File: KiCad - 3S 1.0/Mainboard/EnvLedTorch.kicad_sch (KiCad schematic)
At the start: 73 parts, among them J1 USB_C_Receptacle_USB2.0, J101 Conn_01x02, J102 Conn_01x02, Q1 BSP89, Q2 BSP89, Q3 BSP89, Q4 AO3401A, Q5 AO3401A, SW101 SW_SPST, U1 HY2213, U101 TPS565208, U102 TPS92200, U2 HY2213, U3 HY2213, U4 MT3608, U9 8254

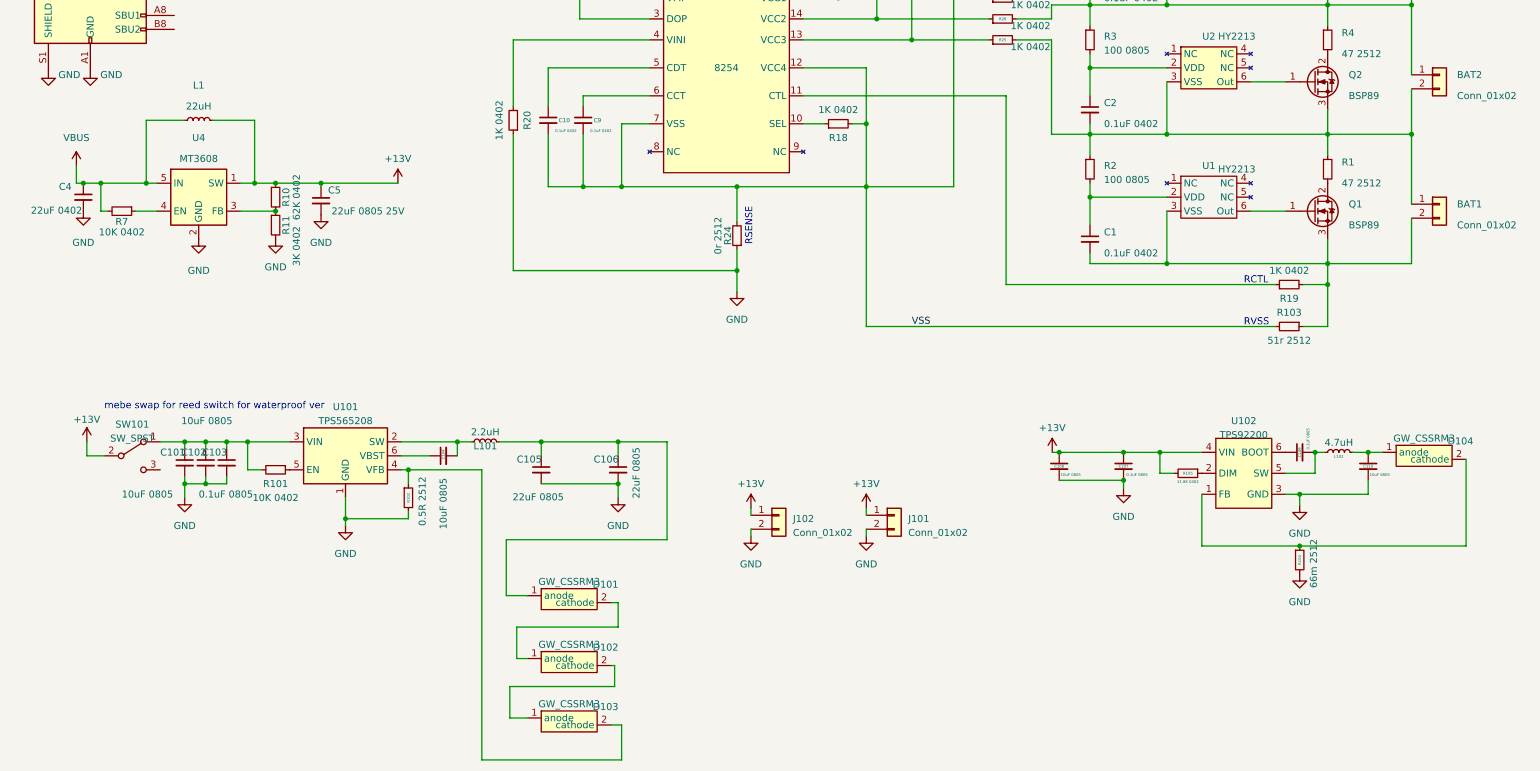
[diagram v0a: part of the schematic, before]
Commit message: broke up 3SV1 into two separate boards (unfinished work)
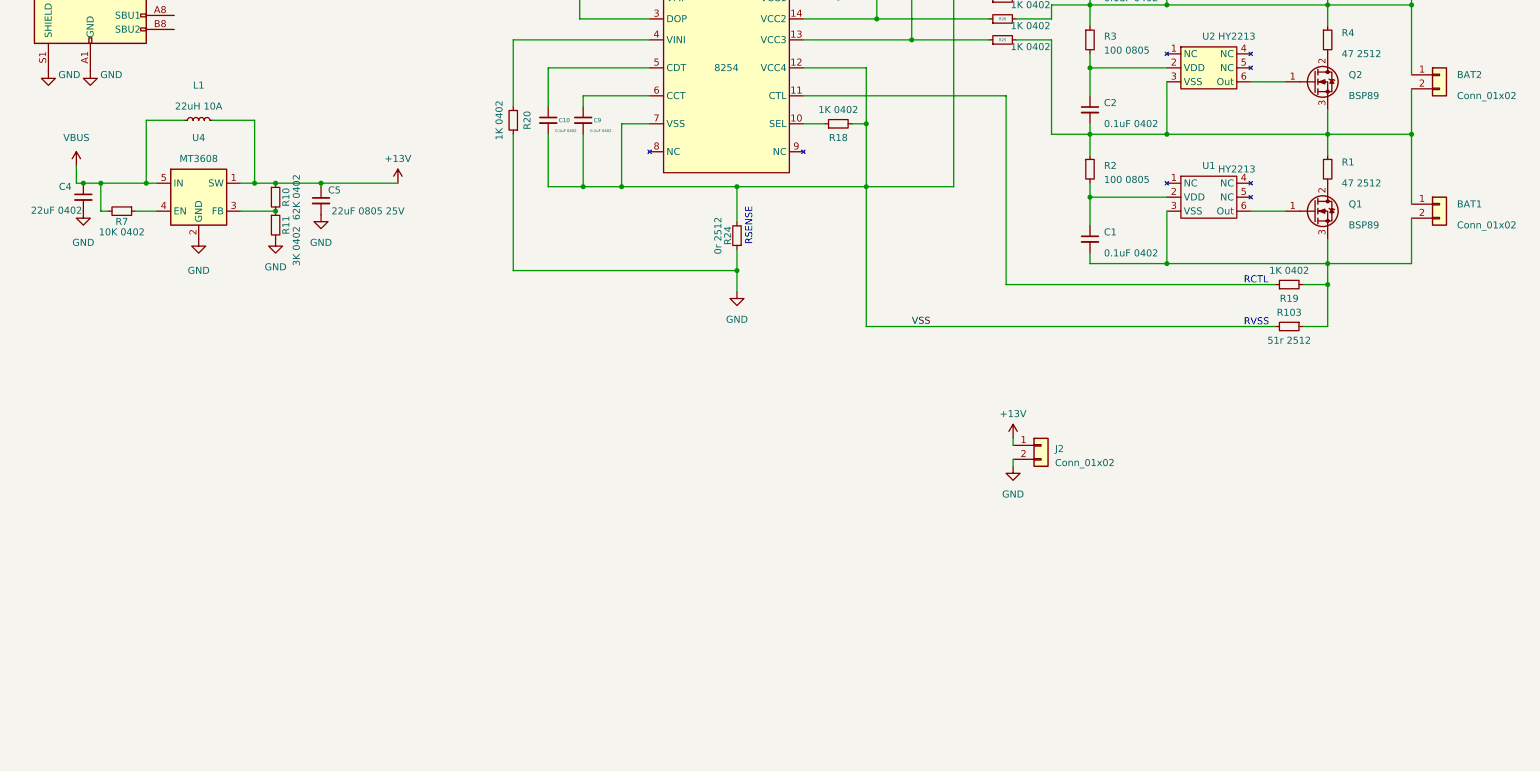
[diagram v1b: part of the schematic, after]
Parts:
- removed C101, C102, C104, C108, C110: 10uF 0805, Capacitor_SMD:C_0805_2012Metric, symbol Device:C_Small
- removed C103, C107, C109: 0.1uF 0805, Capacitor_SMD:C_0805_2012Metric, symbol Device:C_Small
- removed C105, C106: 22uF 0805, Capacitor_SMD:C_0805_2012Metric, symbol Device:C_Small
- removed D101, D102, D103, D104: GW_CSSRM3, GW_CSSRM3:GW_CSSRM3, symbol GW CSSRM3:GW_CSSRM3
- removed J101, J102: Conn_01x02, Connector_Wire:SolderWire-2sqmm_1x02_P7.8mm_D2mm_OD3.9mm, symbol Connector_Generic:Conn_01x02
- removed L101: 2.2uH, Inductor_SMD:L_Sunlord_MWSA0402S, symbol Device:L_Small
- removed L102: 4.7uH, Inductor_SMD:L_Sunlord_MWSA0402S, symbol Device:L_Small
- removed R101: 10K 0402, Resistor_SMD:R_0402_1005Metric, symbol Device:R_Small
- removed R102: 0.5R 2512, Resistor_SMD:R_2512_6332Metric, symbol Device:R_Small
- removed R104: 66m 2512, Resistor_SMD:R_2512_6332Metric, symbol Device:R_Small
- removed R105: 11.8K 0402, Resistor_SMD:R_0402_1005Metric, symbol Device:R_Small
- removed SW101: SW_SPST, Button_Switch_SMD:SW_SPDT_PCM12, symbol Switch:SW_SPDT
- removed U101: TPS565208, Package_TO_SOT_SMD:SOT-23-6, symbol Regulator_Switching:TPS565208
- removed U102: TPS92200, Package_TO_SOT_SMD:SOT-23-6, symbol TPS92200:TPS92200
- added J2: Conn_01x02, Connector_Wire:SolderWire-2sqmm_1x02_P7.8mm_D2mm_OD3.9mm, symbol Connector_Generic:Conn_01x02
- L1: value 22uH -> 22uH 10A; footprint Inductor_SMD:L_Sunlord_MWSA0402S -> Inductor_SMD:L_Sunlord_MWSA0605S
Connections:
- net +12V: now also J2.1 (Pin_1)
- net GND: now also J2.2 (Pin_2)
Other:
- note removed: "mebe swap for reed switch for waterproof ver"

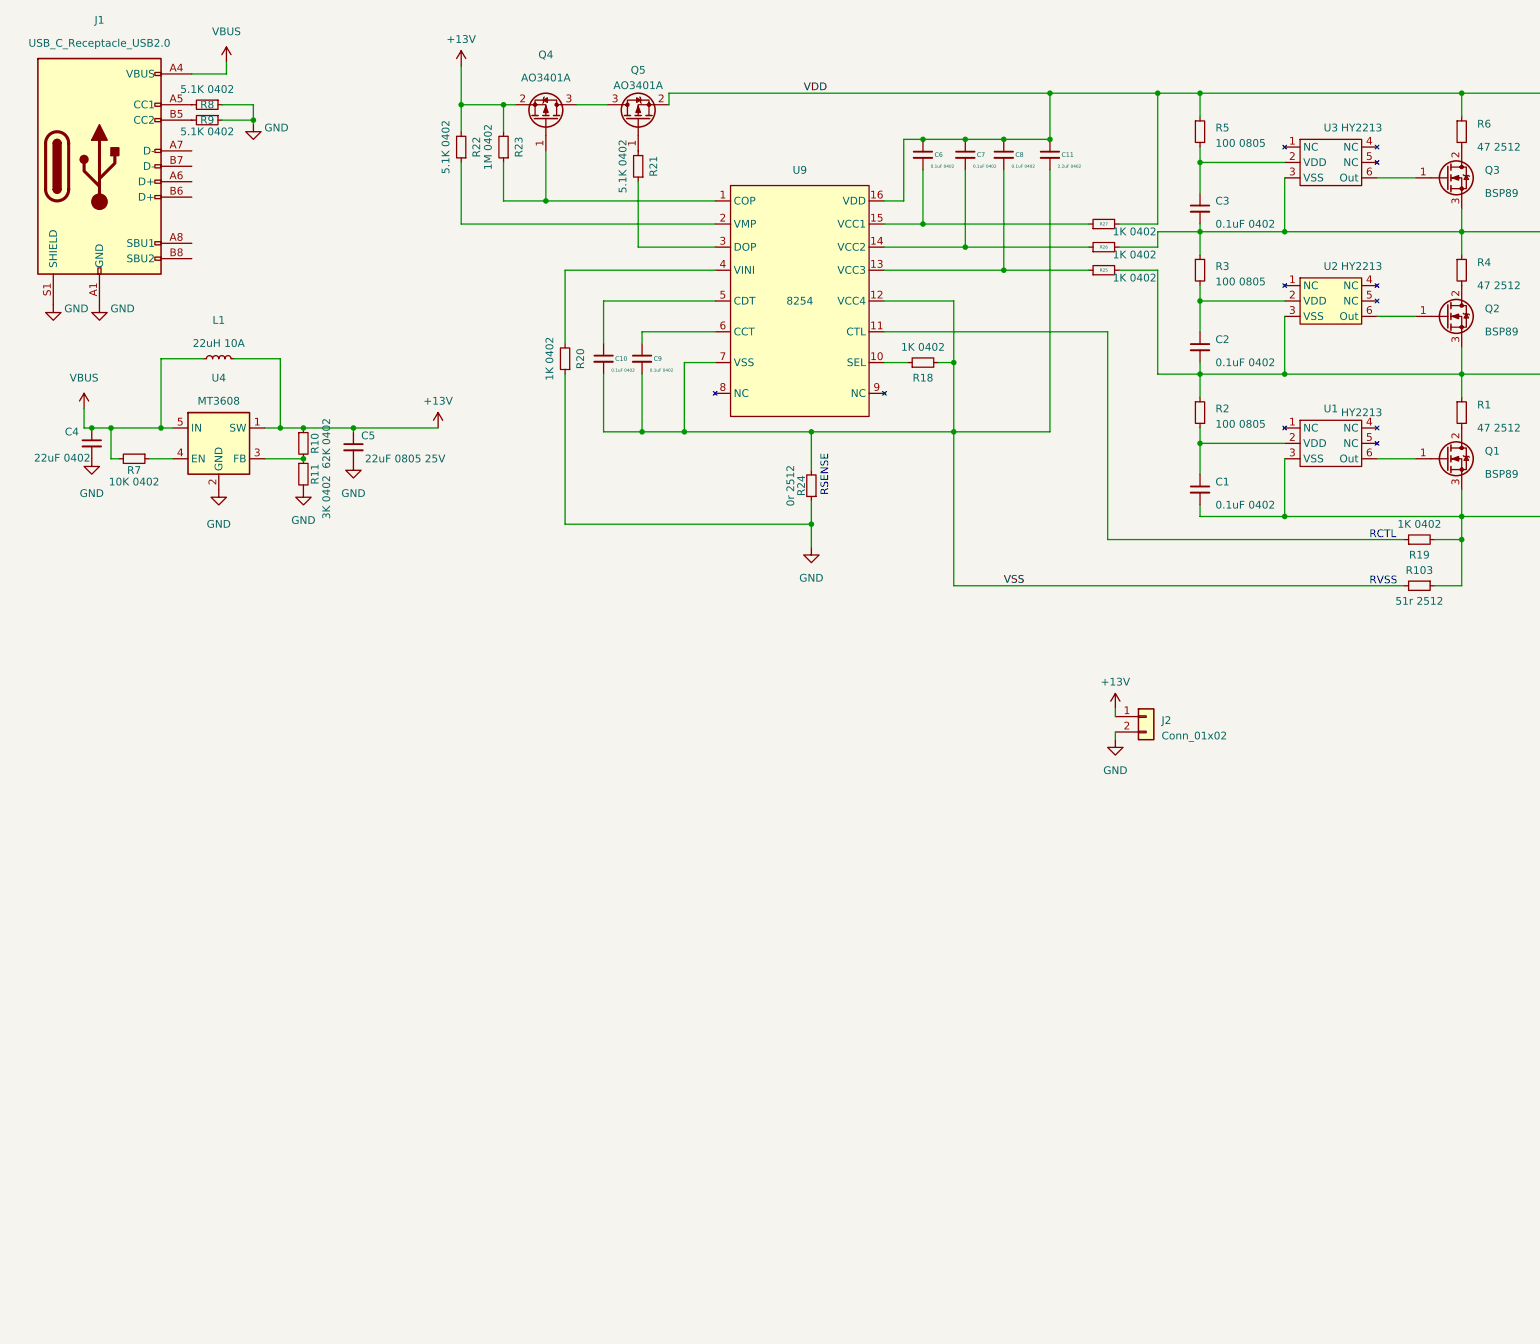
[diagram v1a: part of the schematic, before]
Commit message: started work on adding USB PD 100W support.
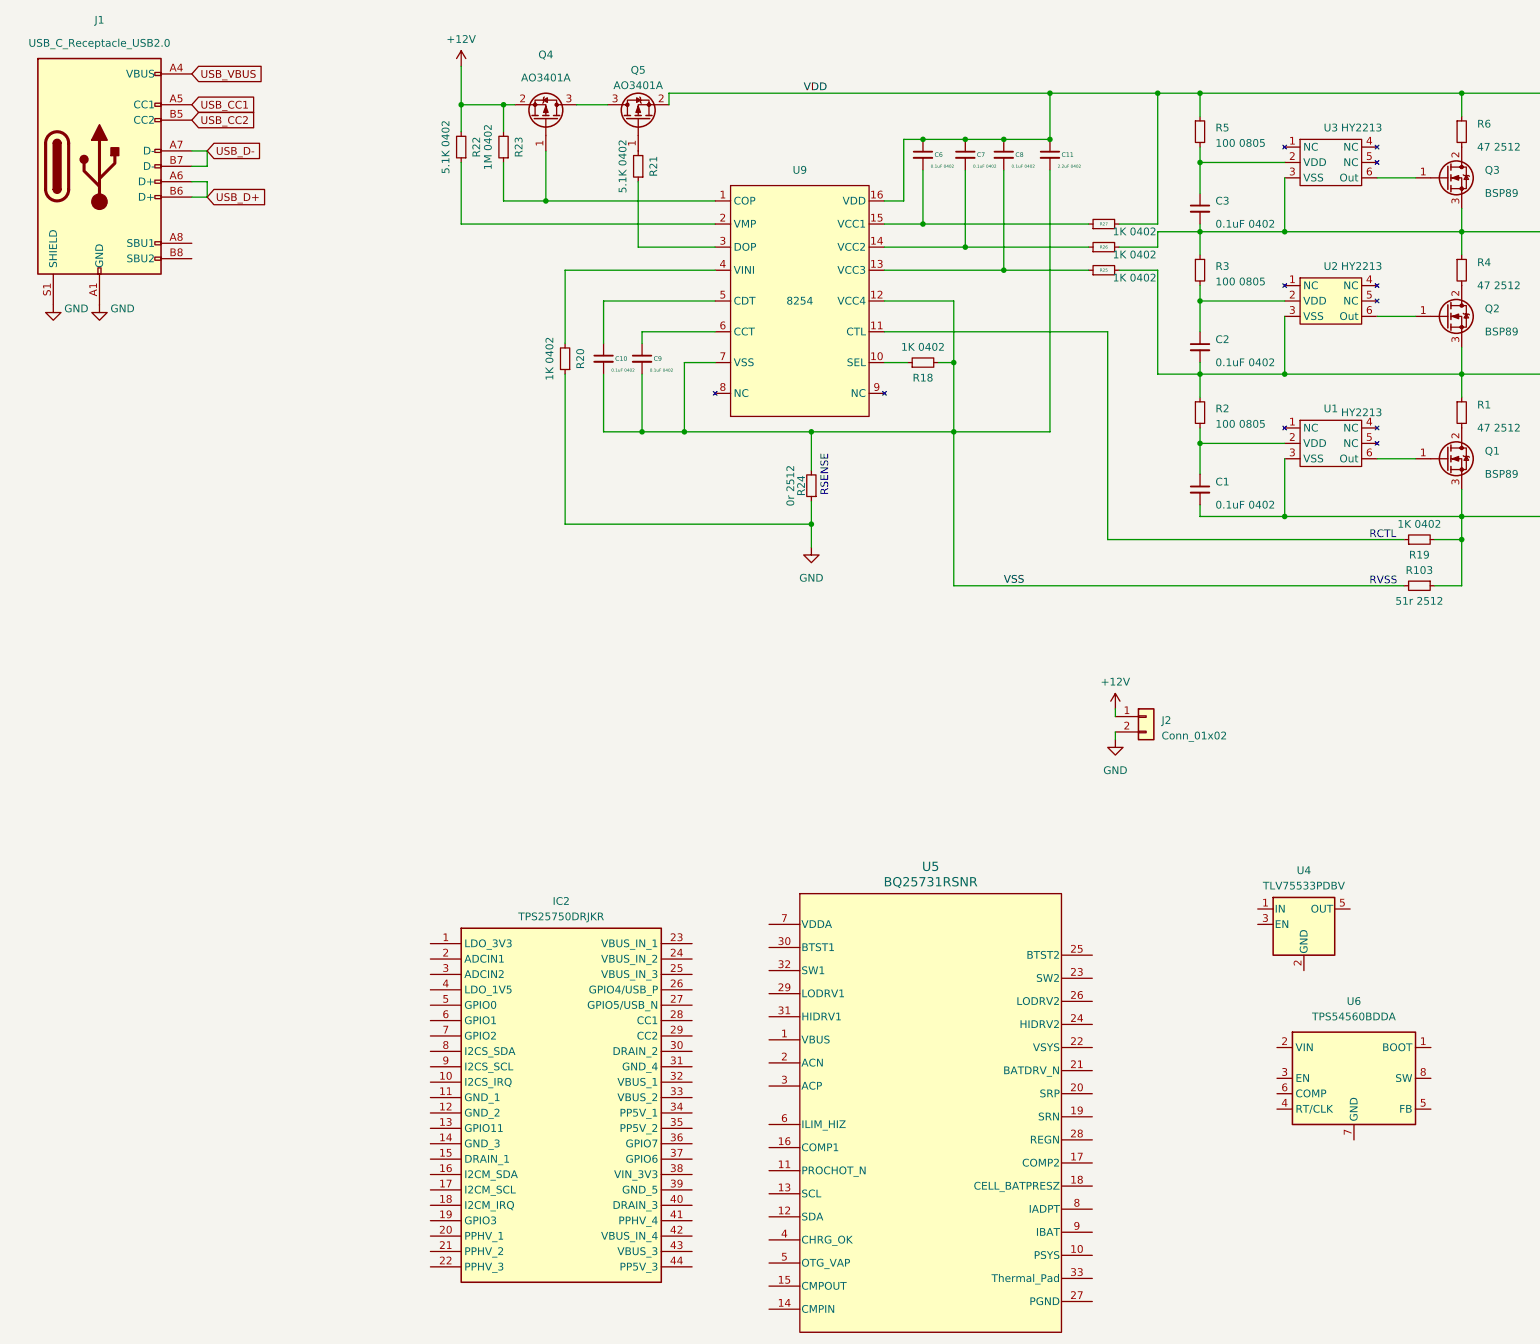
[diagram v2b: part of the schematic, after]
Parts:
- removed C4: 22uF 0402, Capacitor_SMD:C_0402_1005Metric, symbol Device:C_Small
- removed C5: 22uF 0805 25V, Capacitor_SMD:C_0805_2012Metric, symbol Device:C_Small
- removed L1: 22uH 10A, Inductor_SMD:L_Sunlord_MWSA0605S, symbol Device:L_Small
- removed R10: 62K 0402, Resistor_SMD:R_0402_1005Metric, symbol Device:R_Small
- removed R11: 3K 0402, Resistor_SMD:R_0402_1005Metric, symbol Device:R_Small
- removed R7: 10K 0402, Resistor_SMD:R_0402_1005Metric, symbol Device:R_Small
- removed R8, R9: 5.1K 0402, Resistor_SMD:R_0402_1005Metric, symbol Device:R_Small
- removed U4: MT3608, Package_TO_SOT_SMD:SOT-23-6, symbol Regulator_Switching:MT3608
- added IC2: TPS25750DRJKR, TPS25750DRJKR, symbol TPS25750DRJKR:TPS25750DRJKR
- added U4: TLV75533PDBV, Package_TO_SOT_SMD:SOT-23-5, symbol Regulator_Linear:TLV75533PDBV
- added U5: BQ25731RSNR, RSN0032B-IPC_A, symbol BQ25731:BQ25731RSNR
- added U6: TPS54560BDDA, Package_SO:Texas_R-PDSO-G8_EP2.95x4.9mm_Mask2.4x3.1mm_ThermalVias, symbol Regulator_Switching:TPS54560BDDA
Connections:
- net USB_CC1: now reaches J1.A5 (CC1)
- net USB_D+: now reaches J1.A6 (D+)
- net USB_D+: now also J1.B6 (D+)
- net USB_D-: now reaches J1.A7 (D-)
- net USB_D-: now also J1.B7 (D-)
- net USB_CC2: now reaches J1.B5 (CC2)
- net VBUS renamed USB_VBUS
- new net: U6.7 (GND), U6.9 (GND)

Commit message: drew up the schematic to match the reference design from TI for 100W PD charger
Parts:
- removed U5: BQ25731RSNR, RSN0032B-IPC_A, symbol BQ25731:BQ25731RSNR
- removed U6: TPS54560BDDA, Package_SO:Texas_R-PDSO-G8_EP2.95x4.9mm_Mask2.4x3.1mm_ThermalVias, symbol Regulator_Switching:TPS54560BDDA
- added C12, C13, C31, C32, C33, C34, C36, C37, C38: 10uF 0402, Capacitor_SMD:C_0402_1005Metric, symbol Device:C_Small
- added C14, C15: 50V 4.7uF 0402, Capacitor_SMD:C_0402_1005Metric, symbol Device:C_Small
- added C16: 50V 10nF 0402, Capacitor_SMD:C_0402_1005Metric, symbol Device:C_Small
- added C17: 100V 10nF 0402, Capacitor_SMD:C_0402_1005Metric, symbol Device:C_Small
- added C18, C29, C35, C39: 0.1uF 0402, Capacitor_SMD:C_0402_1005Metric, symbol Device:C_Small
- added C19: 50V 2.2nF 0402, Capacitor_SMD:C_0402_1005Metric, symbol Device:C_Small
- added C20: 50V 22pF 0402, Capacitor_SMD:C_0402_1005Metric, symbol Device:C_Small
- added C21: 6.3V 100uF 0402, Capacitor_SMD:C_0402_1005Metric, symbol Device:C_Small
- added C22, C23: 10V 47uF 0402, Capacitor_SMD:C_0402_1005Metric, symbol Device:C_Small
- added C24, C25, C26: 10V 10uF 0402, Capacitor_SMD:C_0402_1005Metric, symbol Device:C_Small
- added C27, C28: 22uF 0402, Capacitor_SMD:C_0402_1005Metric, symbol Device:C_Small
- added C30: 35V 0.1uF 0402, Capacitor_SMD:C_0402_1005Metric, symbol Device:C_Small
- added C4, C5: 330pF 0402, Capacitor_SMD:C_0402_1005Metric, symbol Device:C_Small
- added C40: 4.7uF 0402, Capacitor_SMD:C_0402_1005Metric, symbol Device:C_Small
- added C41, C42: 0.047uF 0402, Capacitor_SMD:C_0402_1005Metric, symbol Device:C_Small
- added C43, C45, C46, C47, C48, C50, C51: 50V 10uF 0402, Capacitor_SMD:C_0402_1005Metric, symbol Device:C_Small
- added C44, C49: 50V 0.1uF 0402, Capacitor_SMD:C_0402_1005Metric, symbol Device:C_Small
- added C52: 50V 1000pF 0402, Capacitor_SMD:C_0402_1005Metric, symbol Device:C_Small
- added D1: CDBC540-G, Diode_SMD:D_SMC, symbol Device:D_Schottky
- added D2: 0402 GREEN, LED_SMD:LED_0402_1005Metric, symbol Device:LED
- added IC1: BQ25792RQMR, BQ25792RQMR:BQ25792RQMR, symbol BQ25792RQMR:BQ25792RQMR
- added J10: 3S/1.5MHz/1A ICGH, Connector_PinHeader_2.54mm:PinHeader_1x02_P2.54mm_Vertical, symbol Connector_Generic:Conn_01x02
- added J11: 4S/1.5MHz/1A ICGH, Connector_PinHeader_2.54mm:PinHeader_1x02_P2.54mm_Vertical, symbol Connector_Generic:Conn_01x02
- added J3, J6: Aardvark, Connector_PinHeader_2.54mm:PinHeader_2x05_P2.54mm_Vertical, symbol Connector_Generic:Conn_02x05_Odd_Even
- added J4: SYS/GND, Connector_PinHeader_2.54mm:PinHeader_1x02_P2.54mm_Vertical, symbol Connector_Generic:Conn_01x02
- added J5: BAT/GND, Connector_PinHeader_2.54mm:PinHeader_1x02_P2.54mm_Vertical, symbol Connector_Generic:Conn_01x02
- added J7: THERMISTOR / GND, Connector_PinHeader_2.54mm:PinHeader_1x02_P2.54mm_Vertical, symbol Connector_Generic:Conn_01x02
- added J8: TS/NORM, Connector_PinHeader_2.54mm:PinHeader_1x02_P2.54mm_Vertical, symbol Connector_Generic:Conn_01x02
- added J9: 2S/1.5MHz/2A ICGH, Connector_PinHeader_2.54mm:PinHeader_1x02_P2.54mm_Vertical, symbol Connector_Generic:Conn_01x02
- added L1: 4.7uH, Inductor_SMD:L_Sunlord_MWSA0804S, symbol Device:L
- added L2: 1uH, Inductor_SMD:L_0805_2012Metric, symbol Device:L
- added NT1: NetTie, NetTie:NetTie-2_SMD_Pad2.0mm, symbol Device:NetTie_2
- added PS1: TPS54531DDAR, TPS54531DDAR:SOIC127P600X170-9N, symbol TPS54531DDAR:TPS54531DDAR
- added R10: 51.1 0402, Resistor_SMD:R_0402_1005Metric, symbol Device:R_Small
- added R11: 10.2K 0402, Resistor_SMD:R_0402_1005Metric, symbol Device:R_Small
- added R12: 1.96K0402, Resistor_SMD:R_0402_1005Metric, symbol Device:R_Small
- added R13, R14, R30, R31, R38: 2.2K 0402, Resistor_SMD:R_0402_1005Metric, symbol Device:R_Small
- added R15, R16, R17, R28, R35: 10K 0402, Resistor_SMD:R_0402_1005Metric, symbol Device:R_Small
- added R29: 100 0402, Resistor_SMD:R_0402_1005Metric, symbol Device:R_Small
- added R32: 10.0 0402, Resistor_SMD:R_0402_1005Metric, symbol Device:R_Small
- added R33: 5.23K 0402, Resistor_SMD:R_0402_1005Metric, symbol Device:R_Small
- added R34: 30.1K 0402, Resistor_SMD:R_0402_1005Metric, symbol Device:R_Small
- added R36: 137K 0402, Resistor_SMD:R_0402_1005Metric, symbol Device:R_Small
- added R37: 100K 0402, Resistor_SMD:R_0402_1005Metric, symbol Device:R_Small
- added R39: 6.04K 0402, Resistor_SMD:R_0402_1005Metric, symbol Device:R_Small
- added R40: 10.5K 0402, Resistor_SMD:R_0402_1005Metric, symbol Device:R_Small
- added R41: 17.4K 0402, Resistor_SMD:R_0402_1005Metric, symbol Device:R_Small
- added R7: 665K 0402, Resistor_SMD:R_0402_1005Metric, symbol Device:R_Small
- added R8: 130K 0402, Resistor_SMD:R_0402_1005Metric, symbol Device:R_Small
- added R9: 37.4K 0402, Resistor_SMD:R_0402_1005Metric, symbol Device:R_Small
- added U6: CAT24C256, Package_SO:MSOP-8-1EP_3x3mm_P0.65mm_EP1.68x1.88mm, symbol Memory_EEPROM:CAT24C256
- IC2: footprint TPS25750DRJKR -> TPS25750DRJKR:TPS25750DRJKR
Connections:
- net GND: now also IC2.10 (I2CS_IRQ), IC2.11 (GND_1), IC2.12 (GND_2), IC2.14 (GND_3), IC2.18 (I2CM_IRQ), IC2.31 (GND_4), IC2.39 (GND_5), U4.2 (GND), C12.2, C13.2, C14.2, C15.2, C16.2, C17.2, C20.2, C21.2, C22.2, C23.2, C24.2, C25.2, C26.2, C27.2, C28.2, C29.2, C30.2, C31.2, C32.2, C33.2, C34.2, C35.2, C36.2, C37.2, C38.2, C39.2, C4.2, C40.2, C43.2, C44.2, C45.2, C46.2, C47.2, C48.2, C49.2, C5.2, C50.2, C51.2, D1.2 (A), IC1.27 (GND), J3.10 (Pin_10), J3.2 (Pin_2), J4.2 (Pin_2), J5.2 (Pin_2), NT1.1, PS1.7 (GND), PS1.9 (EP), R12.1, R15.1, R16.1, R17.1, R28.1, R8.1, R9.1, U6.4 (GND)
- net USB_CC1: now also IC2.28 (CC1), C4.1
- net USB_CC2: now also IC2.29 (CC2), C5.1
- net USB_D+: now also IC2.26 (GPIO4/USB_P)
- net USB_D-: now also IC2.27 (GPIO5/USB_N)
- net USB_VBUS: now also IC2.23 (VBUS_IN_1), IC2.24 (VBUS_IN_2), IC2.25 (VBUS_IN_3), IC2.32 (VBUS_1), IC2.33 (VBUS_2), IC2.42 (VBUS_IN_4), IC2.43 (VBUS_3)
- net LDO_3V3: now reaches IC2.1 (LDO_3V3)
- net LDO_3V3: now also C25.1, C30.1, R13.2, R14.2, R30.2, R31.2, R38.2, U6.8 (VCC)
- net DRAIN: now reaches IC2.15 (DRAIN_1)
- net DRAIN: now also IC2.30 (DRAIN_2), IC2.40 (DRAIN_3)
- net I2C_SDA: now reaches IC2.16 (I2CM_SDA)
- net I2C_SDA: now also IC1.15 (SDA), J3.3 (Pin_3), R14.1, U6.5 (SDA)
- net I2C_SCL: now reaches IC2.17 (I2CM_SCL)
- net I2C_SCL: now also IC1.14 (SCL), J3.1 (Pin_1), R13.1, U6.6 (SCL)
- net LDO_1V5: now reaches IC2.2 (ADCIN1)
- net LDO_1V5: now also IC2.3 (ADCIN2), IC2.4 (LDO_1V5), C26.1
- net PPHV: now reaches IC2.20 (PPHV_1)
- net PPHV: now also IC2.21 (PPHV_2), IC2.22 (PPHV_3), IC2.41 (PPHV_4), C27.1, C28.1, C29.1, C31.1, C32.1, C33.1, C34.1, C35.1, IC1.2 (VBUS_1), IC1.3 (VBUS_2), IC1.31 (VAC1_2), IC1.8 (VAC2), IC1.9 (VAC1_1)
- net PP5V: now reaches IC2.34 (PP5V_1)
- net PP5V: now also IC2.35 (PP5V_2), IC2.44 (PP5V_3), U4.1 (IN), U4.3 (EN), C12.1, C21.1, C22.1, C23.1, L1.2, R10.2
- net P3V3: now reaches IC2.38 (VIN_3V3)
- net P3V3: now also U4.5 (OUT), C13.1, C24.1, R32.2
- net I2C1_SDA: now reaches IC2.8 (I2CS_SDA)
- net I2C1_SDA: now also J6.10 (Pin_10), R30.1
- net I2C1_SCL: now reaches IC2.9 (I2CS_SCL)
- net I2C1_SCL: now also J6.9 (Pin_9), R31.1
- new net: PS1.3 (EN), R7.1, R8.2
- new net: C49.1, C50.1, C51.1, IC1.22 (BAT_1), IC1.23 (BAT_2), J5.1 (Pin_1), R29.1
- new net: C18.1, D1.1 (K), L1.1, PS1.8 (PH)
- new net: IC1.18 (BATP), R29.2
- new net: J8.2 (Pin_2), R35.2
- new net: C18.2, PS1.1 (BOOT)
- new net: C17.1, PS1.4 (SS)
- new net: PS1.5 (VSENSE), R11.1, R12.2
- new net: C19.1, C20.1, PS1.6 (COMP)
- new net: J6.5 (Pin_5), R32.1
- new net: R28.2, U6.7 (WP)
- new net: D2.2 (A), R38.1
- new net: R17.2, U6.1 (A0)
- new net: J10.2 (Pin_2), R40.2
- new net: R16.2, U6.2 (A1)
- new net: R15.2, U6.3 (A2)
- new net: R10.1, R11.2
- new net: J9.2 (Pin_2), R39.2
- new net: J11.2 (Pin_2), R41.2
- new net: C19.2, R9.2
- new net BTST1: C41.1, IC1.4 (BTST1)
- new net BTST2: C42.1, IC1.19 (BTST2)
- new net GNDA: C52.2, IC1.10 (ACDRV2), IC1.11 (ACDRV1), IC1.13 (~{CE}), J6.6 (Pin_6), J7.2 (Pin_2), NT1.2, R34.1, R35.1, R37.1, R39.1, R40.1, R41.1
- new net ILIM_HIZ: IC1.17 (ILIM_HIZ), R36.1, R37.2
- new net PMID: C36.1, C37.1, C38.1, C39.1, IC1.29 (PMID)
- new net PROG: IC1.20 (PROG), J10.1 (Pin_1), J11.1 (Pin_1), J9.1 (Pin_1)
- new net REGN: C40.1, IC1.5 (REGN), R33.2, R36.2
- new net SDRV: C52.1, IC1.24 (SDRV_1), IC1.33 (SDRV_2)
- new net STAT: D2.1 (K), IC1.1 (STAT_1), IC1.30 (STAT_2)
- new net SW1: C41.2, IC1.28 (SW1), L2.1
- new net SW2: C42.2, IC1.26 (SW2), L2.2
- new net SYS: C14.1, C15.1, C16.1, C43.1, C44.1, C45.1, C46.1, C47.1, C48.1, IC1.25 (SYS), J4.1 (Pin_1), PS1.2 (VIN), R7.2
- new net TS: IC1.16 (TS_1), IC1.32 (TS_2), J7.1 (Pin_1), J8.1 (Pin_1), R33.1, R34.2
- no-connect marks 0 -> 22
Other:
- moved on the sheet: BAT1, BAT2, BAT3, C1, C10, C11, C2, C3, C6, C7, C8, C9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
